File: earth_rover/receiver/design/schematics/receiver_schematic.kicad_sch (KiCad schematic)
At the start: 6 parts, among them U2 STM32L432KCUx, U3 TB6612FNG, U4 TB6612FNG, U5 XIAO-ESP32-C3

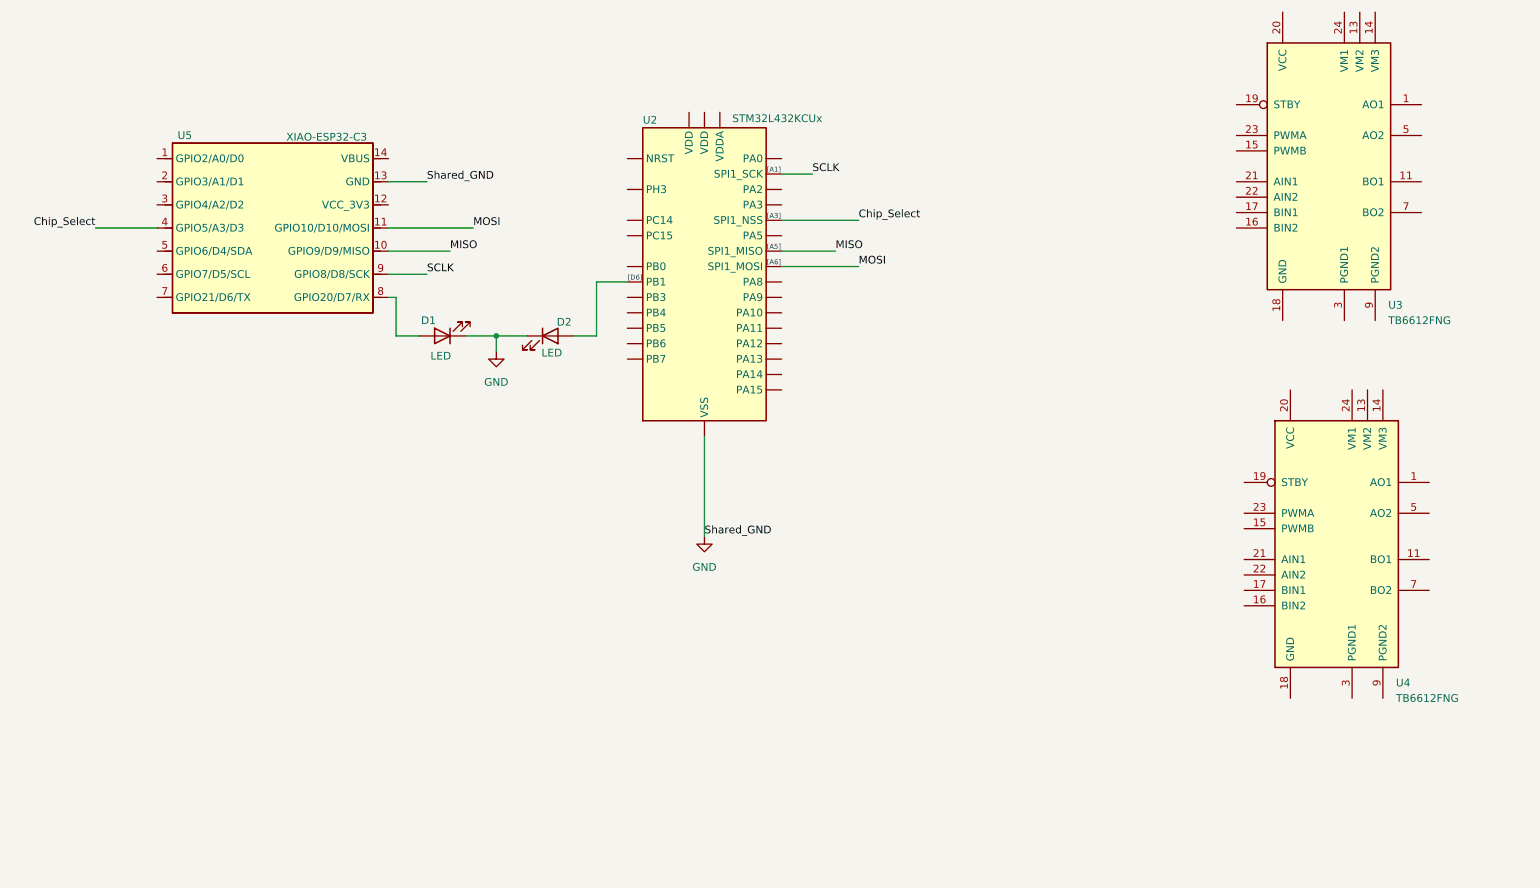
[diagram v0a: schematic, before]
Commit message: Updated The Earth Rover Receiver Schematic
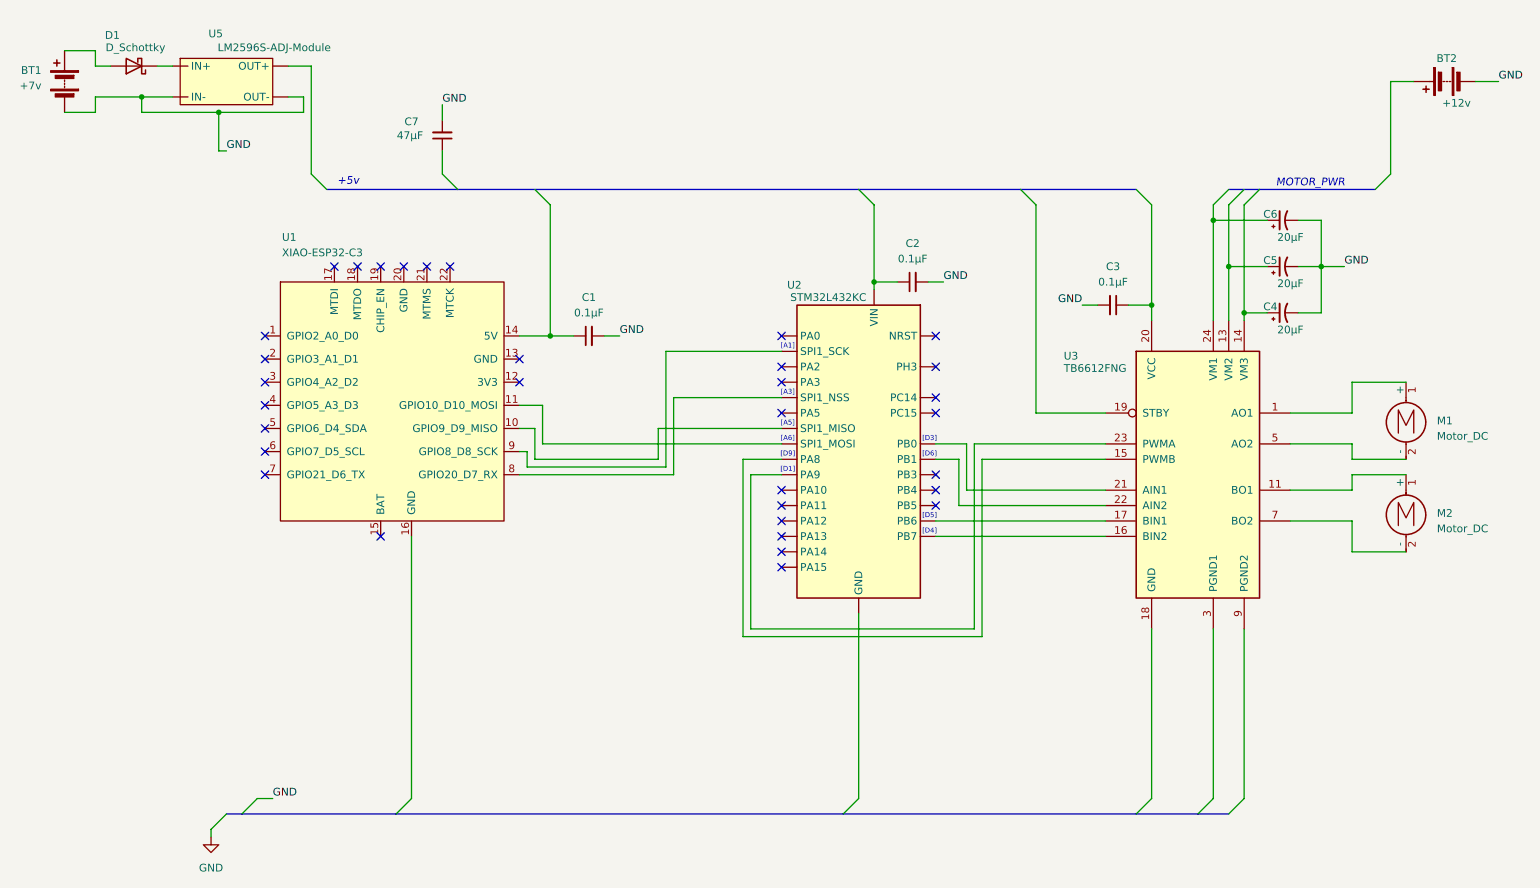
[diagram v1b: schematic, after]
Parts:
- removed D1, D2: LED, symbol Device:LED
- removed U2: STM32L432KCUx, Package_DFN_QFN:QFN-32-1EP_5x5mm_P0.5mm_EP3.45x3.45mm, symbol MCU_ST_STM32L4:STM32L432KCUx
- removed U4: TB6612FNG, Package_SO:SSOP-24_5.3x8.2mm_P0.65mm, symbol Driver_Motor:TB6612FNG
- removed U5: XIAO-ESP32-C3, Module:MOUDLE14P-XIAO-DIP-SMD, symbol Seeed_Studio_XIAO_Series:XIAO-ESP32-C3-DIP
- added BT1: +7v, symbol Device:Battery
- added BT2: +12v, symbol Device:Battery
- added C1, C2, C3: 0.1µF, symbol Device:C_Small
- added C4, C5, C6: 20µF, symbol Device:C_Polarized_Small_US
- added C7: 47µF, symbol Device:C_Small
- added D1: D_Schottky, symbol Device:D_Schottky
- added M1, M2: Motor_DC, symbol Motor:Motor_DC
- added U1: XIAO-ESP32-C3, symbol Seeed_Studio_XIAO_Series:XIAO-ESP32-C3-SMD
- added U2: STM32L432KC, symbol MCU_ST_STM32L4:STM32L432KC-Nucleo
- added U5: LM2596S-ADJ-Module, symbol Regulator_Switching:LM2596S-ADJ-Module
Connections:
- net GND: now also BT1.2 (-), BT2.2 (-), C1.2, C2.2, C3.2, C4.2, C5.2, C6.2, C7.2, U5. (OUT-)
- net at U3.1 (AO1), U3.2 (AO1): now also M1.1 (+)
- net at U3.11 (BO1), U3.12 (BO1): now also M2.1 (+)
- net at U3.13 (VM2): now also C5.1
- net at U3.14 (VM3): now also C4.1
- net at U3.15 (PWMB): now also U2.18 (PA8)
- net at U3.16 (BIN2): now also U2.30 (PB7)
- net at U3.17 (BIN1): now also U2.29 (PB6)
- net at U3.20 (VCC): now also C3.1
- net at U3.21 (AIN1): now also U2.14 (PB0)
- net at U3.22 (AIN2): now also U2.15 (PB1)
- net at U3.23 (PWMA): now also U2.19 (PA9)
- net at U3.24 (VM1): now also C6.1
- net at U3.5 (AO2), U3.6 (AO2): now also M1.2 (-)
- net at U3.7 (BO2), U3.8 (BO2): now also M2.2 (-)
- new net: D1.1 (K), U5. (OUT-)
- new net: C2.1, U2. (GND)
- new net: U1.10 (GPIO9_D9_MISO), U2.12 (PA6)
- new net: U1.11 (GPIO10_D10_MOSI), U2.13 (PA7)
- new net: C1.1, U1.14 (5V)
- new net: U1.8 (GPIO20_D7_RX), U2.10 (PA4)
- new net: U1.9 (GPIO8_D8_SCK), U2.7 (PA1)
- new net: BT1.1 (+), D1.2 (A)
- no-connect marks 0 -> 33
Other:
- note added: "+5v"
- note added: "MOTOR_PWR"
- note added: "[D1]"
- note added: "[D3]"
- note added: "[D4]"
- note added: "[D5]"
- note added: "[D9]"
- moved on the sheet: U3

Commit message: Update Schematic - Receiver
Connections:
- net at U1.4 (GPIO5_A3_D3): now also U2.10 (PA4), U2.9 (PA3)
- net at U1.8 (GPIO20_D7_RX): no longer U2.10 (PA4)
- no-connect marks 33 -> 32
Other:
- note added: "DMA RE-ARM"
- note added: "MOTOR PWR"
- note added: "[A2]"
- note removed: "MOTOR_PWR"
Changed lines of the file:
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@@
 		)
 	)
-	(text "MOTOR_PWR"
+	(text "[A2]\n"
+		(exclude_from_sim no)
+		(at 141.986 89.408 0)
+		(effects
+			(font
+				(size 0.8128 0.8128)
+			)
+		)
+	)
+	(text "MOTOR PWR"
 		(exclude_from_sim no)
 		(at 228.092 57.404 0)
@@
 		)
 	)
+	(text "DMA RE-ARM"
+		(exclude_from_sim no)
+		(at 131.318 89.408 0)
+		(effects
+			(font
+				(size 1.27 1.27)
+				(italic yes)
+				(color 72 72 72 1)
+			)
+		)
+	)
 	(text "[A5]\n"
 		(exclude_from_sim no)
@@
 	)
 	(junction
+		(at 123.19 92.71)
+		(diameter 0)
+		(color 0 0 0 0)
+	)
+	(junction
 		(at 212.09 63.5)
 		(diameter 0)
@@
 	)
 	(no_connect
-		(at 140.97 90.17)
-	)
-	(no_connect
 		(at 71.12 71.12)
 	)
@@
 	)
 	(no_connect
+		(at 97.79 105.41)
+	)
+	(no_connect
 		(at 166.37 87.63)
 	)
@@
 	(no_connect
 		(at 166.37 92.71)
-	)
-	(no_connect
-		(at 55.88 93.98)
 	)
 	(no_connect
@@
 		)
 	)
-	(wire
-		(pts
-			(xy 97.79 105.41) (xy 123.19 105.41)
-		)
-		(stroke
-			(width 0)
-			(type default)
-		)
-	)
 	(bus
 		(pts
@@
 	(wire
 		(pts
+			(xy 123.19 90.17) (xy 123.19 92.71)
+		)
+		(stroke
+			(width 0)
+			(type default)
+		)
+	)
+	(wire
+		(pts
 			(xy 63.5 38.1) (xy 63.5 55.88)
 		)
@@
 	(wire
 		(pts
+			(xy 55.88 93.98) (xy 53.34 93.98)
+		)
+		(stroke
+			(width 0)
+			(type default)
+		)
+	)
+	(wire
+		(pts
 			(xy 97.79 82.55) (xy 102.87 82.55)
 		)
@@
 	(wire
 		(pts
+			(xy 140.97 90.17) (xy 123.19 90.17)
+		)
+		(stroke
+			(width 0)
+			(type default)
+		)
+	)
+	(wire
+		(pts
 			(xy 226.06 71.12) (xy 229.87 71.12)
 		)
@@
 	(wire
 		(pts
+			(xy 53.34 93.98) (xy 53.34 119.38)
+		)
+		(stroke
+			(width 0)
+			(type default)
+		)
+	)
+	(wire
+		(pts
 			(xy 102.87 60.96) (xy 102.87 82.55)
 		)
@@
 	(wire
 		(pts
+			(xy 53.34 119.38) (xy 123.19 119.38)
+		)
+		(stroke
+			(width 0)
+			(type default)
+		)
+	)
+	(wire
+		(pts
 			(xy 193.04 77.47) (xy 190.5 77.47)
 		)
@@
 	(wire
 		(pts
-			(xy 123.19 105.41) (xy 123.19 92.71)
-		)
-		(stroke
+			(xy 123.19 92.71) (xy 123.19 119.38)
+		)
+		(stroke
